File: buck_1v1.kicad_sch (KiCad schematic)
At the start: 14 parts, among them U1 XTPS564257DRLR

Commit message: CuPhy: adding ports
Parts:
- removed R3: 47K, Resistor_SMD:R_0805_2012Metric_Pad1.20x1.40mm_HandSolder, symbol Device:R
- removed R4: 20K, Resistor_SMD:R_0805_2012Metric_Pad1.20x1.40mm_HandSolder, symbol Device:R
- renumbered C19 to C70, C20 to C75, C23 to C76, C24 to C77, C22 to C78, L1 to L4, R1 to R15, R2 to R16, TP1 to TP10, TP2 to TP11, TP3 to TP12, U1 to U4

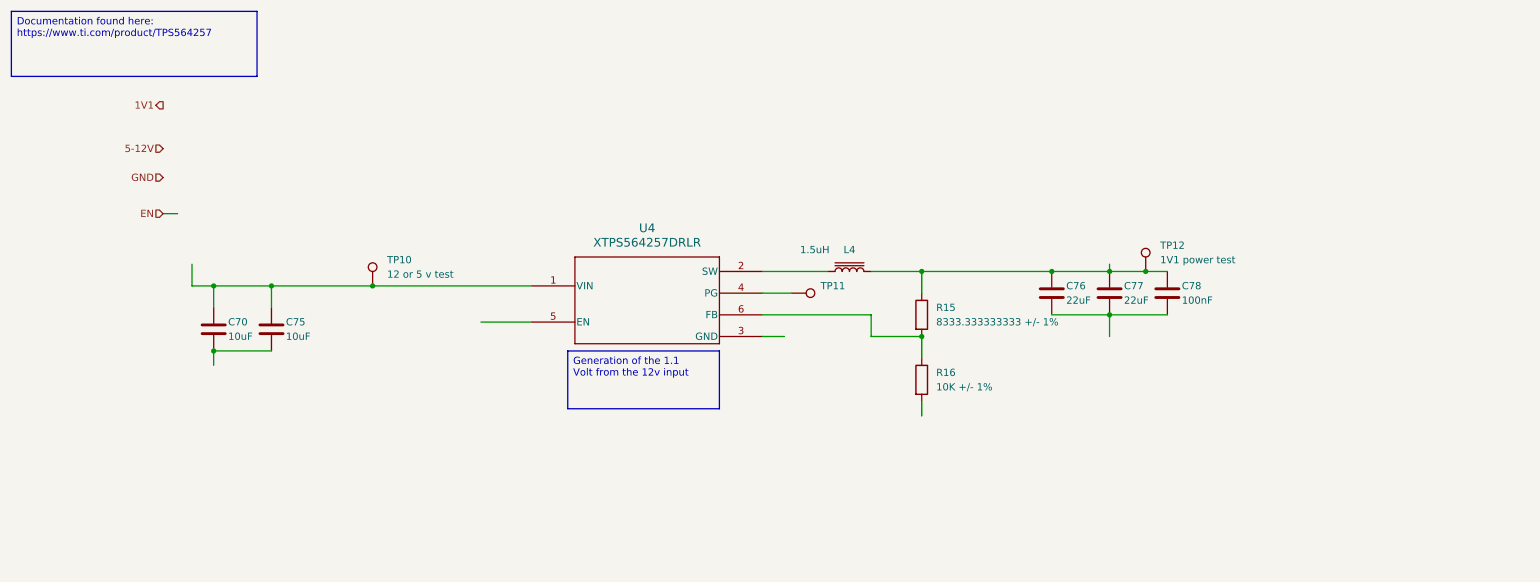
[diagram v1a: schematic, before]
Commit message: schematics: fixing the voltage rail and updating the files
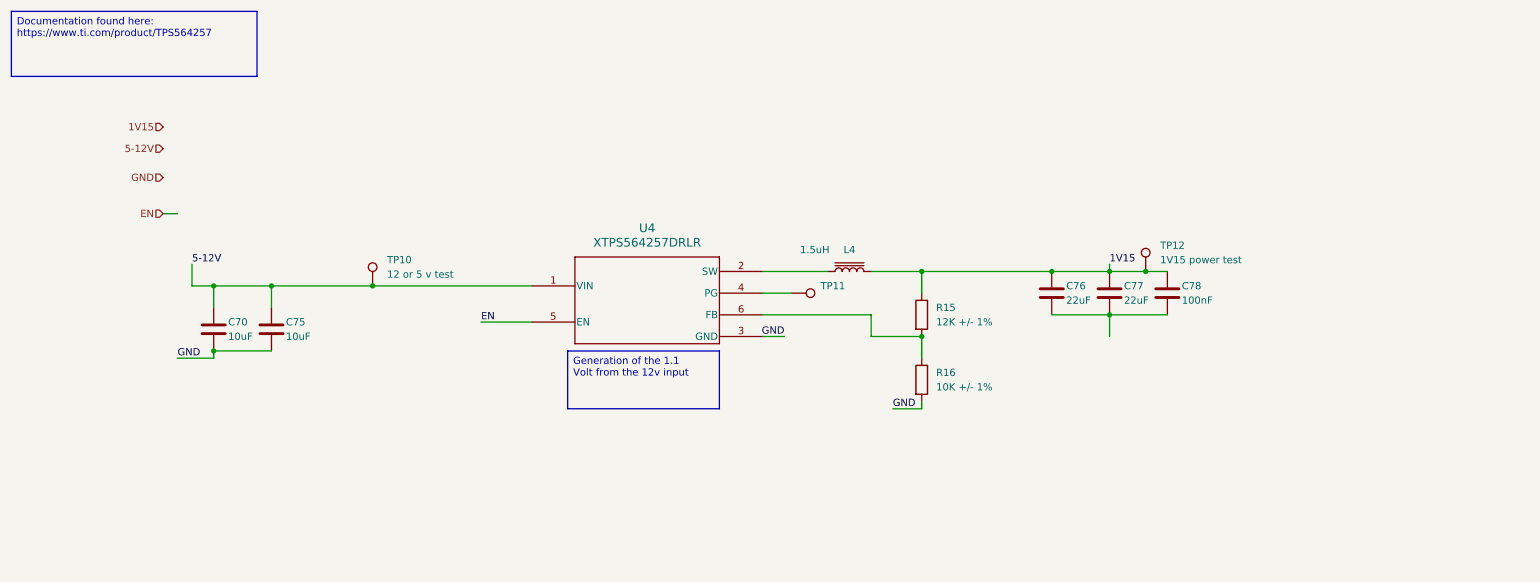
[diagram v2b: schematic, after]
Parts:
- R15: value 8333.333333333 +/- 1% -> 12K +/- 1%
- TP12: value 1V1 power test -> 1V15 power test
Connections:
- net 5-12V: now also C70.1, C75.1, TP10.1, U4.1 (VIN)
- net EN: now also U4.5 (EN)
- net GND: now also C70.2, C75.2, R16.2, U4.3 (GND)
- net 1V15: now reaches C76.1, C77.1, C78.1, L4.2, R15.1, TP12.1

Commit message: switch: finished 1st version
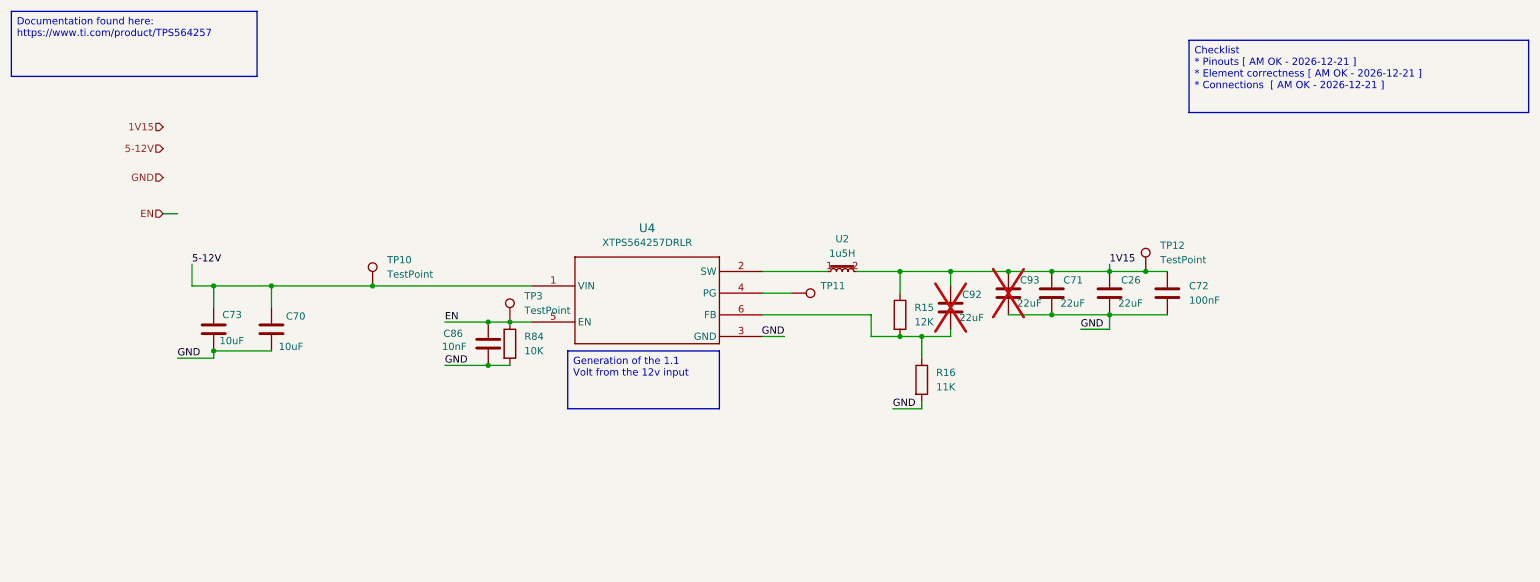
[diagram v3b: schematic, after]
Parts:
- removed C70, C75: 10uF, Capacitor_SMD:C_0805_2012Metric_Pad1.18x1.45mm_HandSolder, symbol Device:C
- removed C76, C77: 22uF, Capacitor_SMD:C_0805_2012Metric_Pad1.18x1.45mm_HandSolder, symbol Device:C
- removed C78: 100nF, Capacitor_SMD:C_0805_2012Metric_Pad1.18x1.45mm_HandSolder, symbol Device:C
- removed L4: 1.5uH, symbol Device:L_Iron
- removed R15: 12K +/- 1%, Resistor_SMD:R_0805_2012Metric_Pad1.20x1.40mm_HandSolder, symbol Device:R
- removed R16: 10K +/- 1%, Resistor_SMD:R_0805_2012Metric_Pad1.20x1.40mm_HandSolder, symbol Device:R
- removed U4: XTPS564257DRLR, TPS564242DRLR_TEX, symbol tps5642:XTPS564257DRLR
- added C26, C71, C92, C93: 22uF, KL:C_0603, symbol KL_C:C_22uF_10V_X5R_0603_20
- added C70, C73: 10uF, KL:C_0603, symbol KL_C:C_10uF_25V_X5R_0603_20
- added C72: 100nF, KL:C_0603, symbol KL_C:C_100nF_10V_X7R_0603_10
- added C86: 10nF, KL:C_0603, symbol KL_C:C_10nF_25V_X7R_0603_20
- added R15: 12K, KL:R_0603, symbol KL_R:R_12K_100mW_1_0603
- added R16: 11K, KL:R_0603, symbol KL_R:R_11K_100mW_1_0603
- added R84: 10K, KL:R_0603, symbol KL_R:R_10K_100mW_5_0603
- added TP3: TestPoint, symbol Connector:TestPoint
- added U2: 1u5H, KL:L_1u5_SRP7050WA, symbol KL_L:L_1u5H_19A
- added U4: XTPS564257DRLR, KL:SOT-563, symbol KL_IC_Power:TI_TPS564357DRLR
- TP10: value 12 or 5 v test -> TestPoint
- TP11: value 12v test -> TestPoint
- TP12: value 1V15 power test -> TestPoint
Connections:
- net 1V15: now also C26.1, C71.1, C72.1, C92.1, C93.1, R15.1, U2.2
- net 5-12V: now also C70.1, C73.1, U4.1 (VIN)
- net EN: now also C86.1, R84.1, TP3.1, U4.5 (EN)
- net GND: now also C26.2, C70.2, C71.2, C72.2, C73.2, C86.2, C93.2, R16.2, R84.2, U4.3 (GND)
- net at TP11.1: now also U4.4 (PG)
- new net: C92.2, R15.2, R16.1, U4.6 (FB)
- new net: U2.1, U4.2 (SW)
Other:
- company: (none) -> Kebag-Logic <contact@kebag-logic.com>
- title: (none) -> Switch 1V15 Power Rail

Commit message: minor footprint fixing
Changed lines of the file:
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@@
 		(fields_autoplaced yes)
 		(property "Reference" "U2"
-			(at 160.02 53.975 0)
+			(at 160.02 53.34 0)
 			(effects
 				(font
@@
 		)
 		(property "Value" "1u5H"
-			(at 160.02 56.515 0)
+			(at 160.02 55.88 0)
 			(effects
 				(font
@@
 			)
 		)
-		(property "Datasheet" "https://www.ti.com/lit/gpn/tps564257"
+		(property "Datasheet" ""
 			(at 125.73 59.69 0)
 			(effects
@@
 		(fields_autoplaced yes)
 		(property "Reference" "TP11"
-			(at 156.21 62.2299 90)
-			(effects
-				(font
+			(at 156.21 63.4999 90)
+			(effects
+				(font

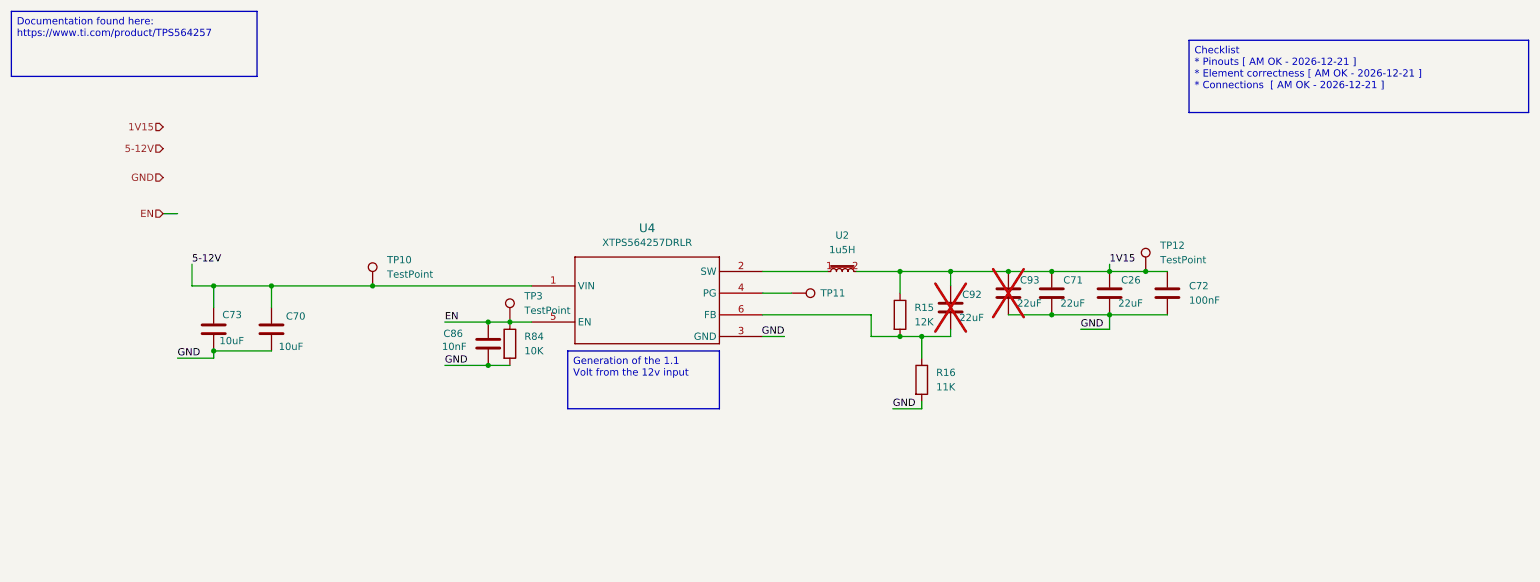
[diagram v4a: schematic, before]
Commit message: review of +1V1 converter
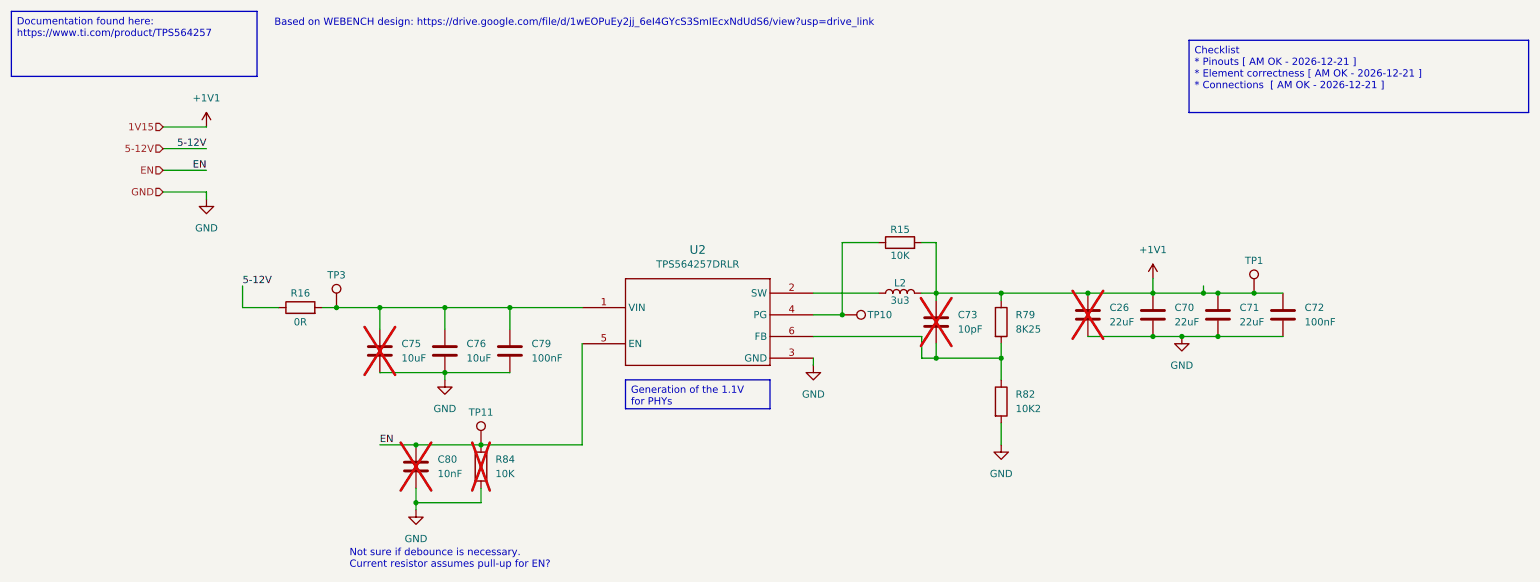
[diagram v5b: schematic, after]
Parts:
- removed C70, C73: 10uF, KL:C_0603, symbol KL_C:C_10uF_25V_X5R_0603_20
- removed C86: 10nF, KL:C_0603, symbol KL_C:C_10nF_25V_X7R_0603_20
- removed C92, C93: 22uF, KL:C_0603, symbol KL_C:C_22uF_10V_X5R_0603_20
- removed R15: 12K, KL:R_0603, symbol KL_R:R_12K_100mW_1_0603
- removed R16: 11K, KL:R_0603, symbol KL_R:R_11K_100mW_1_0603
- removed TP10, TP11, TP12, TP3: TestPoint, symbol Connector:TestPoint
- removed U2: 1u5H, KL:L_1u5_SRP7050WA, symbol KL_L:L_1u5H_19A
- removed U4: XTPS564257DRLR, KL:SOT-563, symbol KL_IC_Power:TI_TPS564357DRLR
- added C70: 22uF, KL:C_0603, symbol KL_C:C_22uF_10V_X5R_0603_20
- added C73: 10pF, Capacitor_SMD:C_0201_0603Metric, symbol KL_C:C_10pF_25V_C0G_0603_5
- added C75, C76: 10uF, KL:C_0603, symbol KL_C:C_10uF_25V_X5R_0603_20
- added C79: 100nF, KL:C_0603, symbol KL_C:C_100nF_16V_X7R_0603_10
- added C80: 10nF, KL:C_0603, symbol KL_C:C_10nF_25V_X7R_0603_20
- added L2: 3u3, KL:L_3u3_EXLA1V0603, symbol KL_L:L_3u3_8A
- added R15: 10K, KL_Footprints:C_0603, symbol KL_R:R_10K_100mW_5_0603
- added R16: 0R, KL_Footprints:R_2512, symbol KL_R:R_0R_2W_5_2512
- added R79: 8K25, symbol KL_R:R_8K25_63mW_1_0402
- added R82: 10K2, KL:R_0603, symbol KL_R:R_10K2_100mW_1_0603
- added TP1, TP10, TP11, TP3: ~, Connector_PinHeader_2.54mm:PinHeader_1x01_P2.54mm_Vertical, symbol KL_TP:TestPoint
- added U2: TPS564257DRLR, KL:SOT-563, symbol KL_IC_Power:TI_TPS564357DRLR
- C26, R84: now not fitted; now left out of the parts list
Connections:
- net 5-12V: now also R16.1
- net EN: now also C80.1, TP11.1, U2.5 (EN)
- net GND: now also C70.2, C75.2, C76.2, C79.2, C80.2, R82.2, U2.3 (GND)
- net 1V15 renamed +1V1
- net +1V1: now also C70.1, C73.1, L2.2, R15.2, R79.1, TP1.1
- new net: R15.1, TP10.1, U2.4 (PG)
- new net: C75.1, C76.1, C79.1, R16.2, TP3.1, U2.1 (VIN)
- new net: C73.2, R79.2, R82.1, U2.6 (FB)
- new net: L2.1, U2.2 (SW)
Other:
- note added: "Based on WEBENCH design: https://drive.google.com/file/d/1wEOPuEy2jj_6eI4GYcS3SmIEcxNdUdS6/view?usp=drive_link"
- note added: "Not sure if debounce is necessary. Current resistor assumes pull-up for EN?"
